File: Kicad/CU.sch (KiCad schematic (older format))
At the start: 40 parts, among them U11 74HCT139, U12 74HCT153, U13 74HCT138, U14 74HCT138, U15 74HCT240, U16 74HCT32

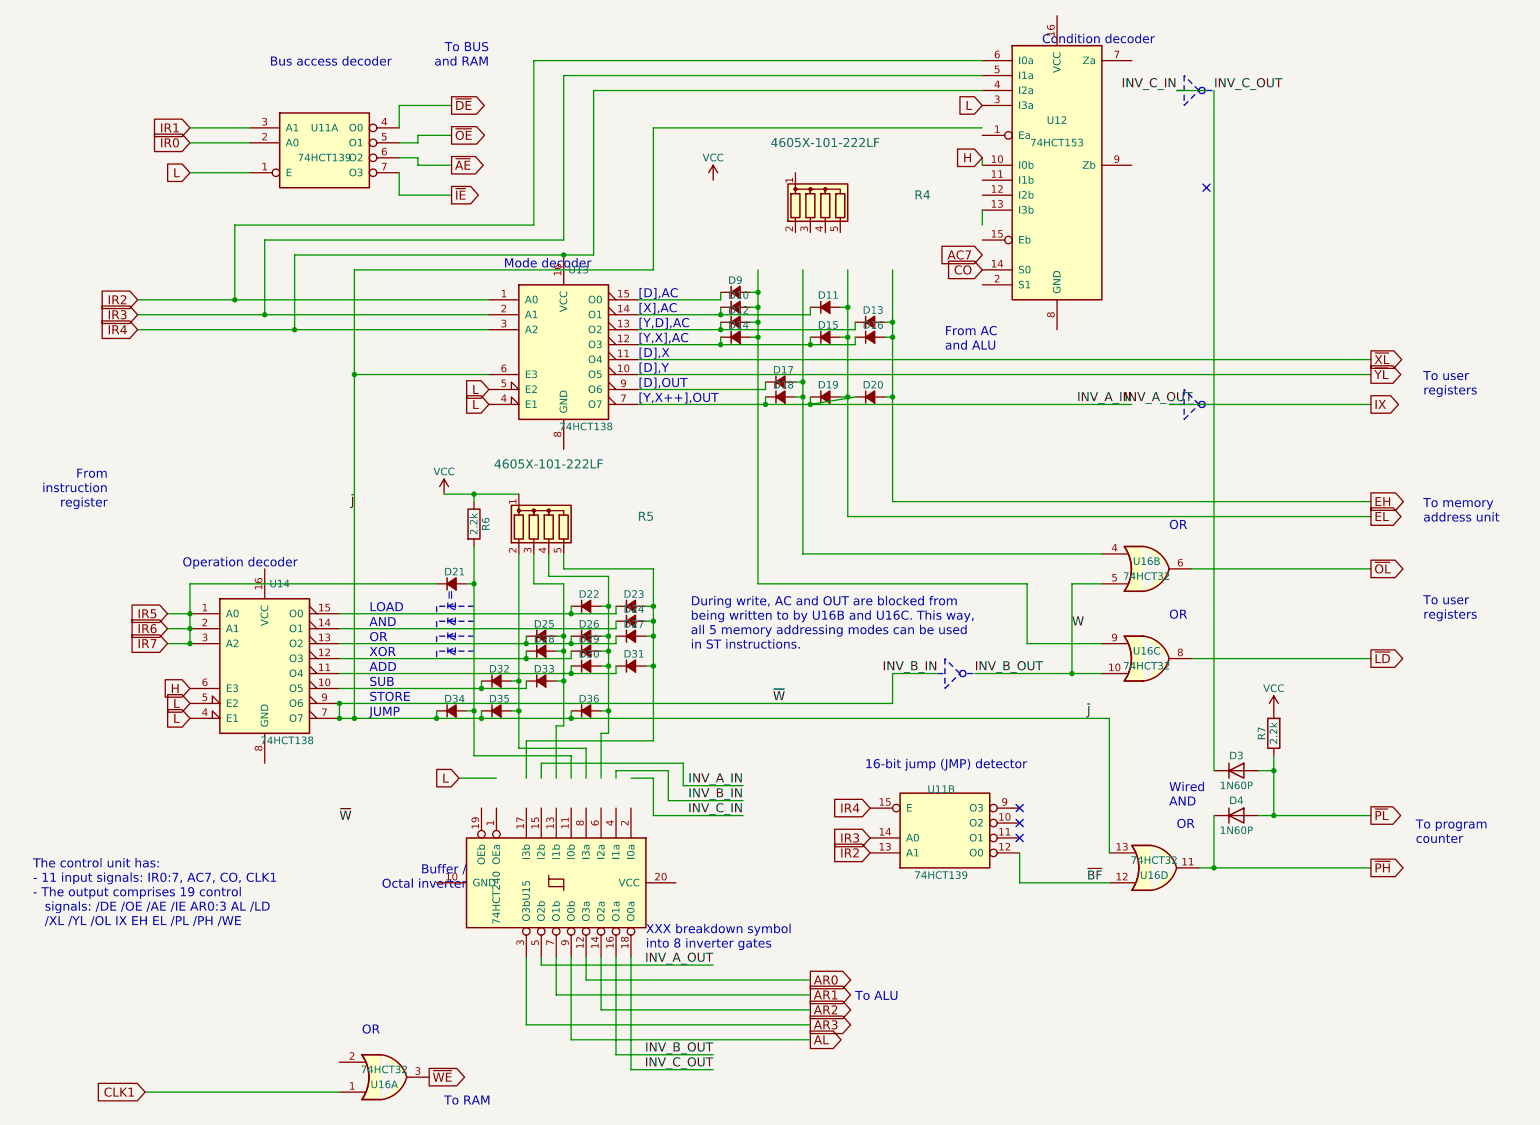
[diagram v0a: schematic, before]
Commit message: Update to work with mostly the default KiCAD items or items downloaded via the KiCAD Libraries too.
2 Resistors added of 1k on the lines for TRUE and FALSE pull ups.

Several things deleted which appeared at Graphic shapes on the PCB sometimes
but could not be edited. this was done manually at the bottom of the PCB_KiCAD file.

Deleted some PCB items around the order which marked the Copper limits of top and bottom. may have been tied to TRUE & FALSE.

Changed USB socket type.

This has been done not to change the board but to aid understanding and allow anyone who wants slightly easier access.

I have not tested it and provide no warranty.

Signed-off-by: John Bradley <flypie@rocketmail.com>
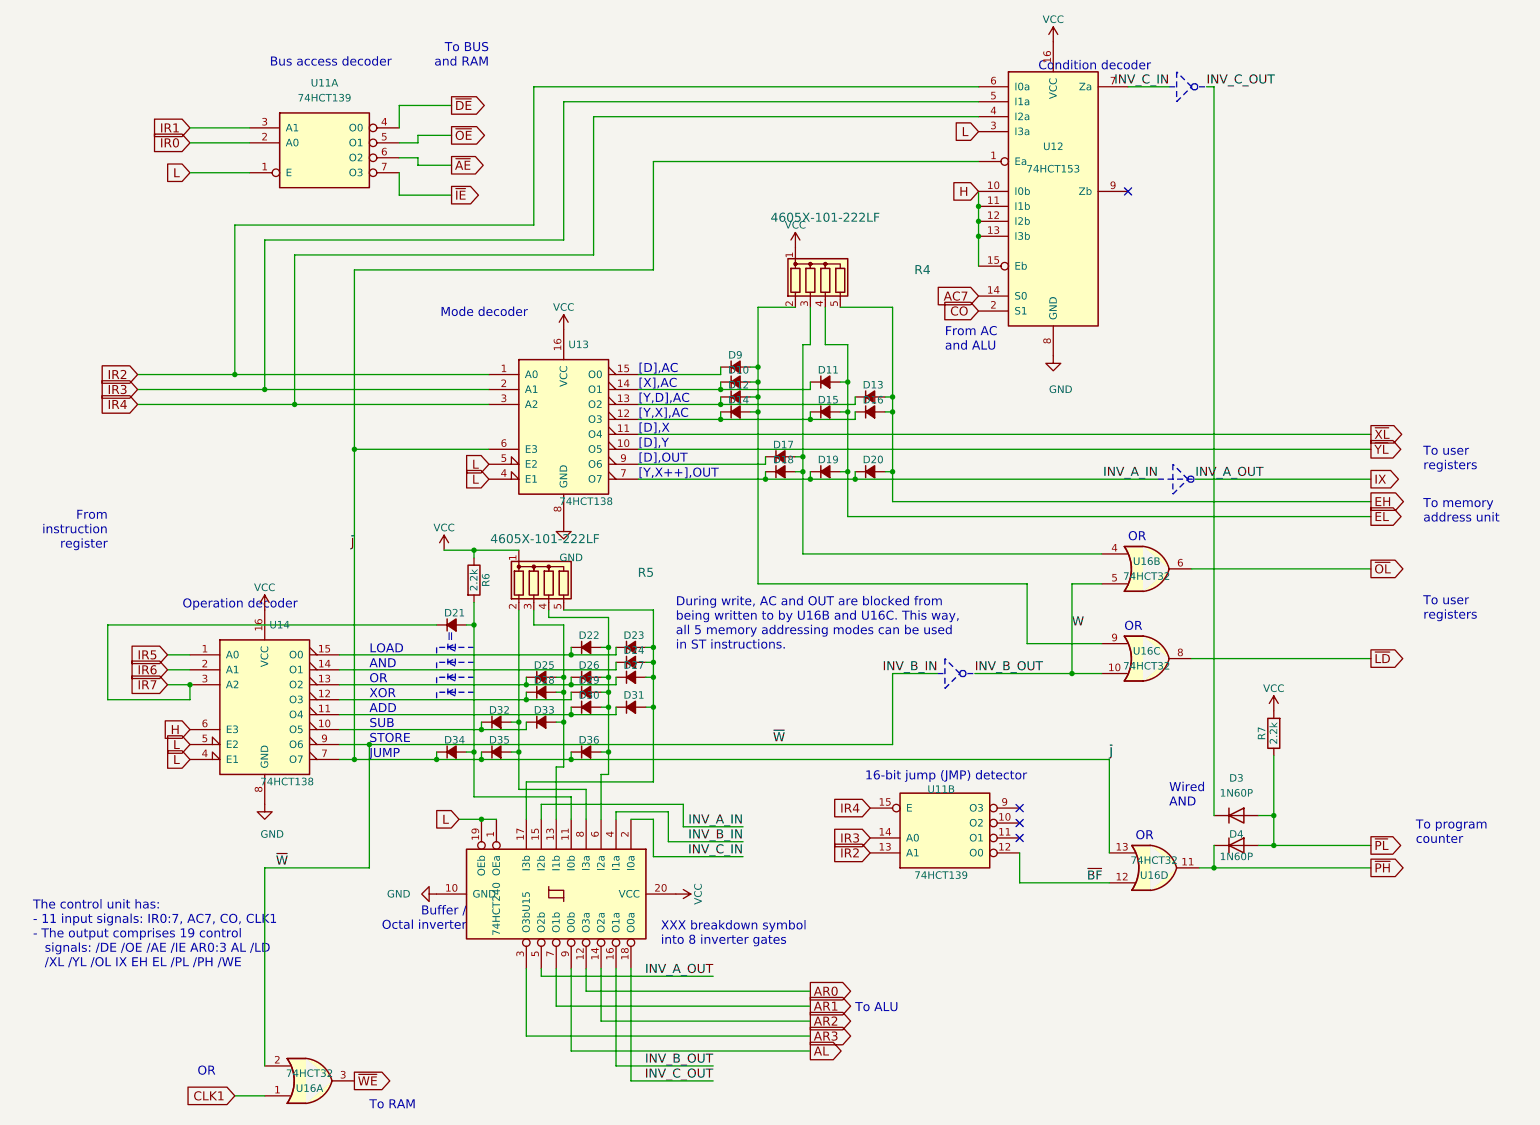
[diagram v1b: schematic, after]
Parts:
- D10, D11, D12, D13, D14, D15, D16, D17, D18, D19, D20, D21, D22, D23, D24, D25, D26, D27, D28, D29, D30, D31, D32, D33, D34, D35, D36, D9: footprint Diodes_THT:D_A-405_P2.54mm_Vertical_KathodeUp -> Diode_THT:D_A-405_P2.54mm_Vertical_KathodeUp
- D3, D4: footprint Diodes_THT:D_A-405_P7.62mm_Horizontal -> Diode_THT:D_A-405_P7.62mm_Horizontal
- R4, R5: footprint Resistors_THT:R_Array_SIP5 -> Resistor_THT:R_Array_SIP5
- R6, R7: footprint Resistors_THT:R_Axial_DIN0207_L6.3mm_D2.5mm_P10.16mm_Horizontal -> Resistor_THT:R_Axial_DIN0207_L6.3mm_D2.5mm_P10.16mm_Horizontal
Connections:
- net labels added: GND
- wire segments 248 -> 260
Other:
- moved on the sheet: D10, D11, D12, D13, D14, D15, D16, D17, D18, D19, D20, D21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
